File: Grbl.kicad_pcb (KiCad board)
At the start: 2 copper layers, 68.5 x 56.6 mm, 32 parts, among them P1 CTL, P2 MISC, P3 STEP, P4 SPIN, P5 LIMIT, P6 GND, P7 GND

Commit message: Correct silkscreen for spindle pins
These accidentially had the PWM_SPIN and DIR_SPIN labels swapped.
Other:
- board text added: "PWM_SPIN EN_SPIN DIR_SPIN"
- board text removed: "DIR_SPIN EN_SPIN PWM_SPIN"
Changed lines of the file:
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@@
     (effects (font (size 1.5 1.5) (thickness 0.3)))
   )
-  (gr_text "DIR_SPIN\nEN_SPIN\nPWM_SPIN" (at 162.56 81.28) (layer F.SilkS)
+  (gr_text "PWM_SPIN\nEN_SPIN\nDIR_SPIN" (at 162.56 81.28) (layer F.SilkS)
     (effects (font (size 1.6 1.5) (thickness 0.3)) (justify left))
   )

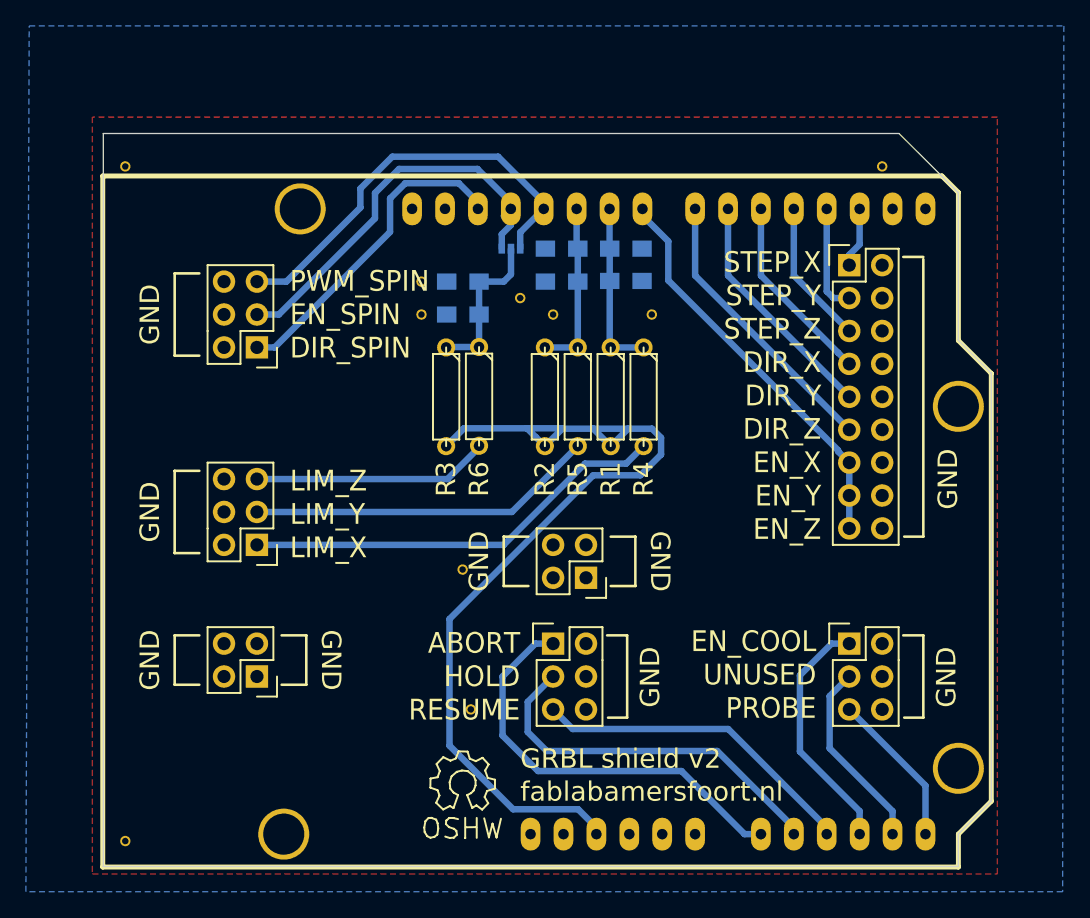
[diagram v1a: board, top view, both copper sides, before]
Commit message: Convert design to KiCad 5, with some changes
This converts the design to use the newer KiCad 5 symbols and
footprints, but additionally makes some changes:
 - The Arduino Uno symbol is now one from the default library instead of a
   third-party symbol, but it has a different pin numbering and layout.
 - The limit pin filtering schematic is a bit more spaced out, using net
   labels instead of direct connections.
 - The Arduino Uno footprint is now one from the default library and has
   two extra pins. It also has smaller mounting holes, see
   https://github.com/KiCad/kicad-footprints/issues/590
 - The solder jumper used was not available anymore, so a bigger one was
   used instead.
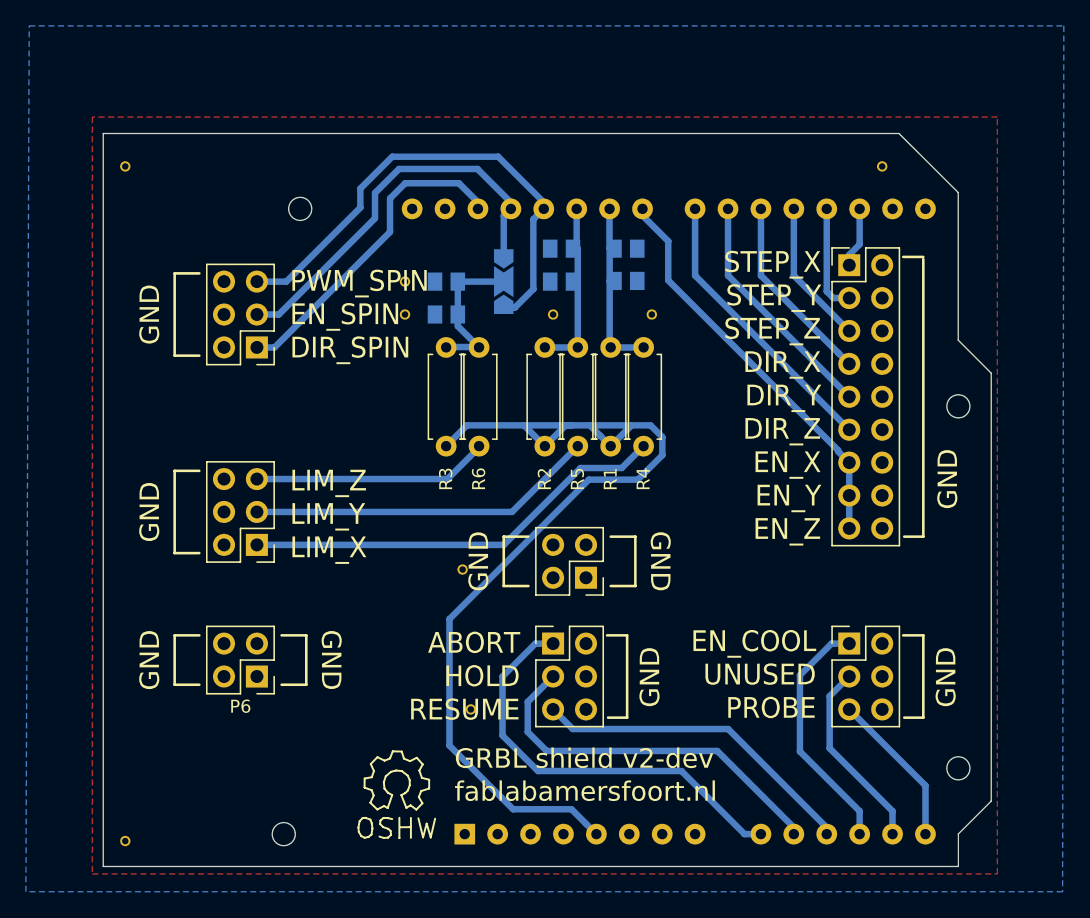
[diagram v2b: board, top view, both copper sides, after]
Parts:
- removed the REF** at (180.3, 80.0)
- C1, C2, C3, C4, C5, C6: footprint Capacitors_SMD:C_0805_HandSoldering -> Capacitor_SMD:C_0805_2012Metric
- JP1: footprint Footprints:S_JUMPER_3 -> Jumper:SolderJumper-3_P2.0mm_Open_TrianglePad1.0x1.5mm_NumberLabels
- P1, P2, P4, P5: footprint Pin_Headers:Pin_Header_Straight_2x03 -> Connector_PinHeader_2.54mm:PinHeader_2x03_P2.54mm_Vertical
- P3: footprint Pin_Headers:Pin_Header_Straight_2x09 -> Connector_PinHeader_2.54mm:PinHeader_2x09_P2.54mm_Vertical
- P6, P7: footprint Pin_Headers:Pin_Header_Straight_2x02 -> Connector_PinHeader_2.54mm:PinHeader_2x02_P2.54mm_Vertical
- R1, R2, R3, R4, R5, R6: footprint Discret:R3 -> Resistor_THT:R_Axial_DIN0207_L6.3mm_D2.5mm_P7.62mm_Horizontal
- SHIELD1: footprint Arduino:ARDUINO_SHIELD -> Module:Arduino_UNO_R2_WithMountingHoles; moved to B.Cu
- moved SHIELD1 28.1 mm to (176.1, 121.4)
- moved REF** 5.08 mm to (170.8, 117.5)
- moved R1 3.81 mm to (187.3, 83.8)
- moved R2 3.81 mm to (182.2, 83.8)
- moved R3 3.81 mm to (174.6, 83.8)
- moved R4 3.81 mm to (189.9, 83.8)
- moved R5 3.81 mm to (184.8, 83.8)
- moved R6 3.78 mm to (177.2, 83.8)
- moved JP1 2.60 mm to (179.1, 78.7), turned to 90 degrees
- moved REF** 1.27 mm to (171.4, 78.7)
- moved REF** 1.27 mm to (171.4, 81.3)
- moved C5 1.27 mm to (174.6, 78.7)
- moved C6 1.27 mm to (174.6, 81.3)
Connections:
- net Net-(C5-Pad1) renamed /LIM_Z_FILTERED
- C1 pad 1: Net-(C1-Pad1) -> /LIM_X_FILTERED
- C2 pad 1: Net-(C1-Pad1) -> /LIM_X_FILTERED
- C3 pad 1: Net-(C3-Pad1) -> /LIM_Y_FILTERED
- C4 pad 1: Net-(C3-Pad1) -> /LIM_Y_FILTERED
- P3 pad 12: GND -> Net-(P3-Pad12)
- P3 pad 14: GND -> Net-(P3-Pad14)
- P3 pad 16: GND -> Net-(P3-Pad16)
- P3 pad 18: GND -> Net-(P3-Pad18)
- P3 pad 2: GND -> Net-(P3-Pad2)
- P3 pad 4: GND -> Net-(P3-Pad4)
- P3 pad 6: GND -> Net-(P3-Pad6)
- P3 pad 8: GND -> Net-(P3-Pad8)
- P4 pad 2: GND -> Net-(P4-Pad2)
- P4 pad 6: GND -> Net-(P4-Pad6)
- P5 pad 2: GND -> Net-(P5-Pad2)
- P5 pad 6: GND -> Net-(P5-Pad6)
- R1 pad 1: Net-(C1-Pad1) -> /LIM_X_FILTERED
- R2 pad 1: Net-(C3-Pad1) -> /LIM_Y_FILTERED
- R4 pad 1: Net-(C1-Pad1) -> /LIM_X_FILTERED
- R5 pad 1: Net-(C3-Pad1) -> /LIM_Y_FILTERED
- SHIELD1 pad : GND -> (no net)
- SHIELD1 pad 10: Net-(C3-Pad1) -> /HOLD
- SHIELD1 pad 11: /PWM_SPIN -> /RESUME
- SHIELD1 pad 12: /EN_SPIN -> /EN_COOL
- SHIELD1 pad 13: /DIR_SPIN -> /UNUSED
- SHIELD1 pad 2: /STEP_X -> Net-(SHIELD1-Pad2)
- SHIELD1 pad 3: /STEP_Y -> Net-(SHIELD1-Pad3)
- SHIELD1 pad 4: /STEP_Z -> Net-(SHIELD1-Pad4)
- SHIELD1 pad 5: /DIR_X -> +5V
- SHIELD1 pad 6: /DIR_Y -> GND
- SHIELD1 pad 7: /DIR_Z -> GND
- SHIELD1 pad 8: /EN_X -> Net-(SHIELD1-Pad8)
- SHIELD1 pad 9: Net-(C1-Pad1) -> /ABORT
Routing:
- net Net-(C1-Pad1): track 13.4 -> 0.00 mm
- net /LIM_X_FILTERED: track 0.00 -> 13.4 mm
- net Net-(C3-Pad1): track 13.3 -> 0.00 mm
- net /LIM_Y_FILTERED: track 0.00 -> 13.3 mm
- net /PWM_SPIN: track 33.3 -> 38.9 mm
- net +5V: track 72.3 -> 74.2 mm
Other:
- board text added: "GRBL shield v2-dev"
- board text removed: "GRBL shield v2"
